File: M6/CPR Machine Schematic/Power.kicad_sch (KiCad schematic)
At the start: 51 parts, among them J1 Contactor 22.2V IN, J2 5V Spare Headers, J3 Power Switch, J4 3V3 Spare Headers, J5 12 Spare headers, J6 Battery Spare headers, J7 GND Spare Headers, Q1 2N3904, Q2 AO3407A, Q4 DMMT5401 PNP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

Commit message: PCB V2 Part 2
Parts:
- C1, C5, C7: footprint Capacitor_SMD:C_1206_3216Metric -> Capacitor_SMD:C_1206_3216Metric_Pad1.33x1.80mm_HandSolder; now left out of the parts list
- C10: footprint Capacitor_SMD:C_1206_3216Metric -> Capacitor_SMD:C_1206_3216Metric_Pad1.33x1.80mm_HandSolder; digikey (none) -> 311-4461-1-ND
- C11: footprint Capacitor_SMD:C_1206_3216Metric -> Capacitor_SMD:C_1206_3216Metric_Pad1.33x1.80mm_HandSolder; digikey (none) -> 732-8099-1-ND
- C12: footprint Capacitor_SMD:C_1206_3216Metric -> Capacitor_SMD:C_1206_3216Metric_Pad1.33x1.80mm_HandSolder; digikey (none) -> 732-8122-1-ND
- C2: footprint Capacitor_SMD:C_1206_3216Metric -> Capacitor_THT:CP_Radial_D10.0mm_P5.00mm; digikey (none) -> 565-EGXF161ELL510MJ20S-ND
- C3: footprint Capacitor_SMD:C_1206_3216Metric -> Capacitor_SMD:C_1206_3216Metric_Pad1.33x1.80mm_HandSolder; digikey (none) -> 399-C1206C220K5HACTUCT-ND
- C4, C6, C8, C9: footprint Capacitor_SMD:C_1206_3216Metric -> Capacitor_SMD:C_1206_3216Metric_Pad1.33x1.80mm_HandSolder; digikey (none) -> 1276-1072-1-ND
- D2: value B220 -> B220a; footprint Diode_SMD:D_SMB -> Diode_SMD:D_SMA_Handsoldering; digikey (none) -> B220A-FDICT-ND
- D3: footprint Diode_SMD:D_SMA -> Diode_SMD:D_SMB_Handsoldering; digikey (none) -> 1801-SS24CT-ND
- F1: footprint Fuse:Fuse_1206_3216Metric -> Fuse:Fuse_1206_3216Metric_Pad1.42x1.75mm_HandSolder; digikey (none) -> 5923-C1F5CT-ND
- J1, J3: digikey (none) -> 277-1667-ND
- J2, J4, J5, J6, J7, TP1, TP2, TP3, TP4: now left out of the parts list
- L1: digikey (none) -> 513-1432-1-ND
- L2: value 5 uH -> 6.8 uH; digikey (none) -> 118-SRU8043-6R8YCT-ND
- LED1, LED2, LED3, LED4: digikey (none) -> 160-1179-1-ND
- Q1: footprint Package_TO_SOT_THT:TO-92_Inline -> Package_TO_SOT_THT:TO-92_Inline_Wide; digikey (none) -> 2N3904FS-ND
- Q2: digikey (none) -> 785-1006-1-ND
- Q4: digikey (none) -> DMMT5401-FDICT-ND
- R1, R4: value 50 kOhm -> 49.9 kOhm; footprint Resistor_SMD:R_1206_3216Metric -> Resistor_SMD:R_1206_3216Metric_Pad1.30x1.75mm_HandSolder; digikey (none) -> 311-49.9KFRCT-ND
- R10: value 660 Ohm -> 665 Ohm; footprint Resistor_SMD:R_1206_3216Metric -> Resistor_SMD:R_1206_3216Metric_Pad1.30x1.75mm_HandSolder; digikey (none) -> 311-665FRCT-ND
- R11, R12, R13: footprint Resistor_SMD:R_1206_3216Metric -> Resistor_SMD:R_1206_3216Metric_Pad1.30x1.75mm_HandSolder; now left out of the parts list
- R14, R8: footprint Resistor_SMD:R_1206_3216Metric -> Resistor_SMD:R_1206_3216Metric_Pad1.30x1.75mm_HandSolder; digikey (none) -> A129830CT-ND
- R2: footprint Resistor_SMD:R_1206_3216Metric -> Resistor_SMD:R_1206_3216Metric_Pad1.30x1.75mm_HandSolder; digikey (none) -> 118-CR1206-FX-3571ELFCT-ND
- R3: footprint Resistor_SMD:R_1206_3216Metric -> Resistor_SMD:R_1206_3216Metric_Pad1.30x1.75mm_HandSolder; digikey (none) -> RMCF1206FT20K0CT-ND
- R7: footprint Resistor_SMD:R_1206_3216Metric -> Resistor_SMD:R_1206_3216Metric_Pad1.30x1.75mm_HandSolder; digikey (none) -> RMCF1206FT2K00CT-ND
- R9: value 1.4 kOhm -> 1.5 kOhm; footprint Resistor_SMD:R_1206_3216Metric -> Resistor_SMD:R_1206_3216Metric_Pad1.30x1.75mm_HandSolder; digikey (none) -> RMCF1206JG1K50CT-ND
- U1: digikey (none) -> 505-LT1765EFE-5#PBF-ND
- U2: digikey (none) -> 505-MAX42402AFLB+-ND
- U4: digikey (none) -> 1951-2739-ND
- U6: digikey (none) -> 1951-2742-ND

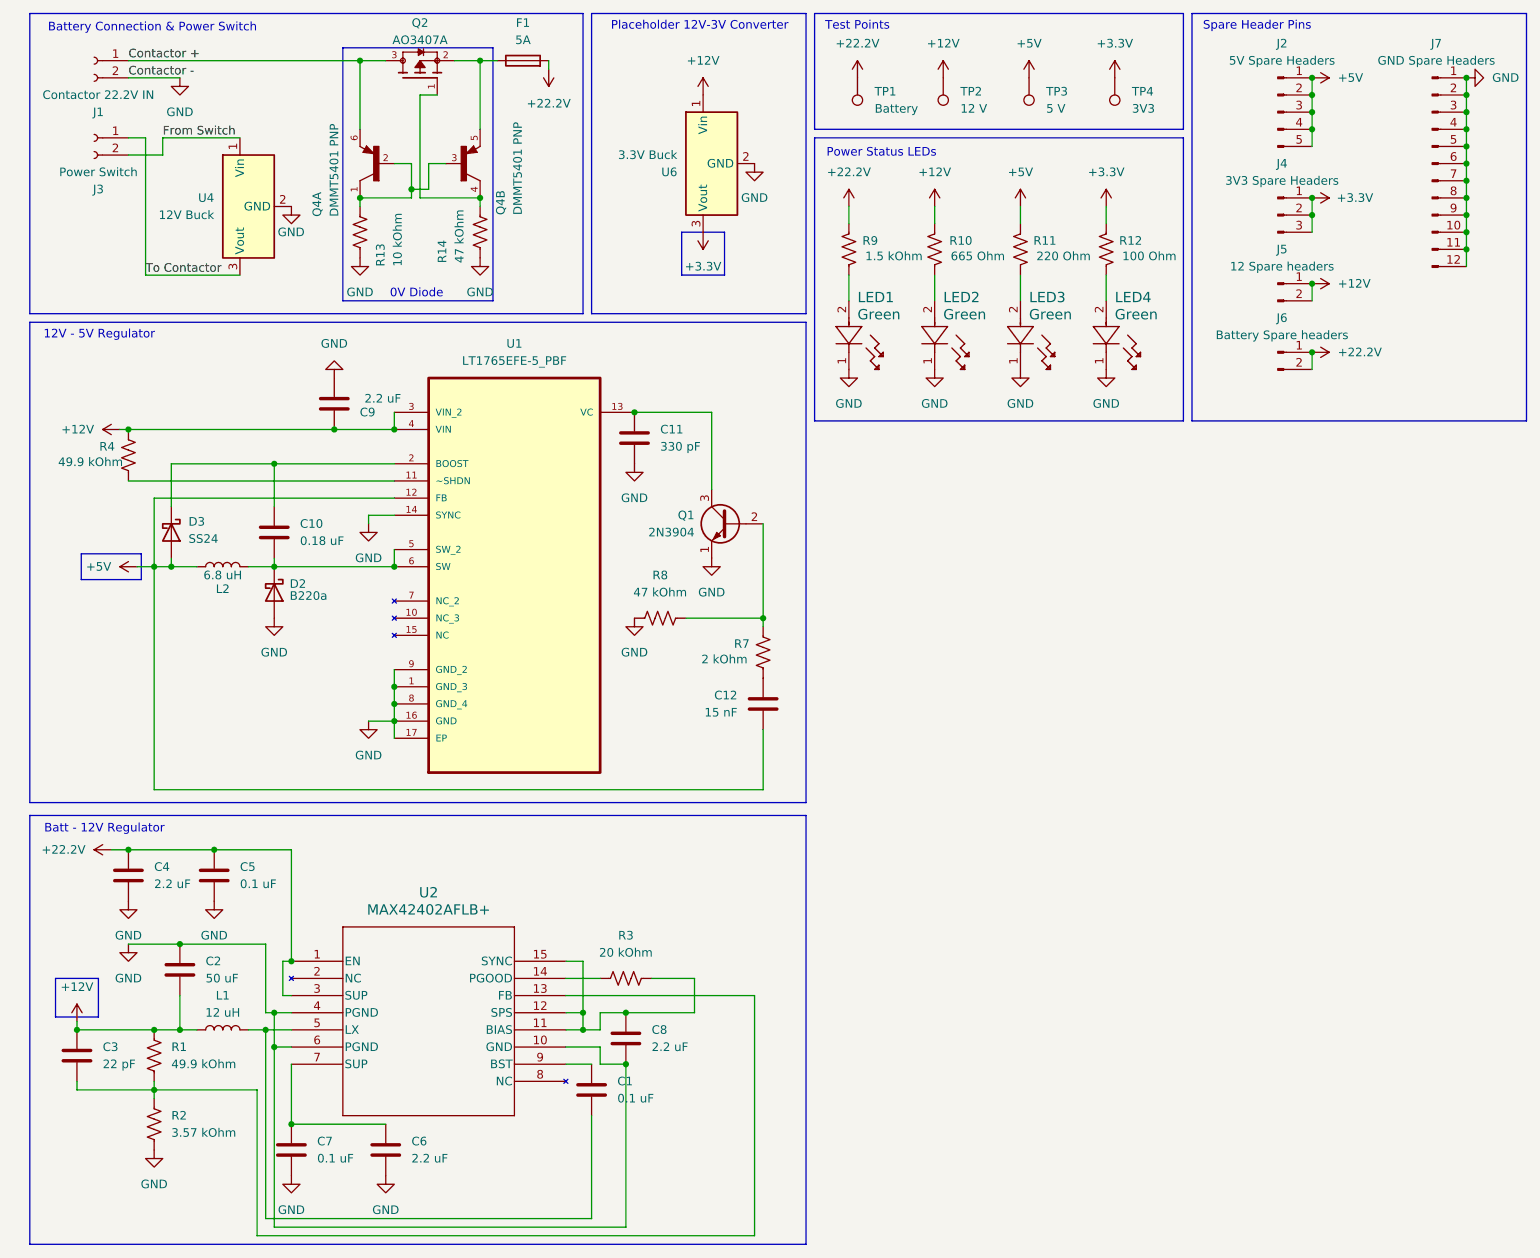
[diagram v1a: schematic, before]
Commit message: Down with the second buck converter
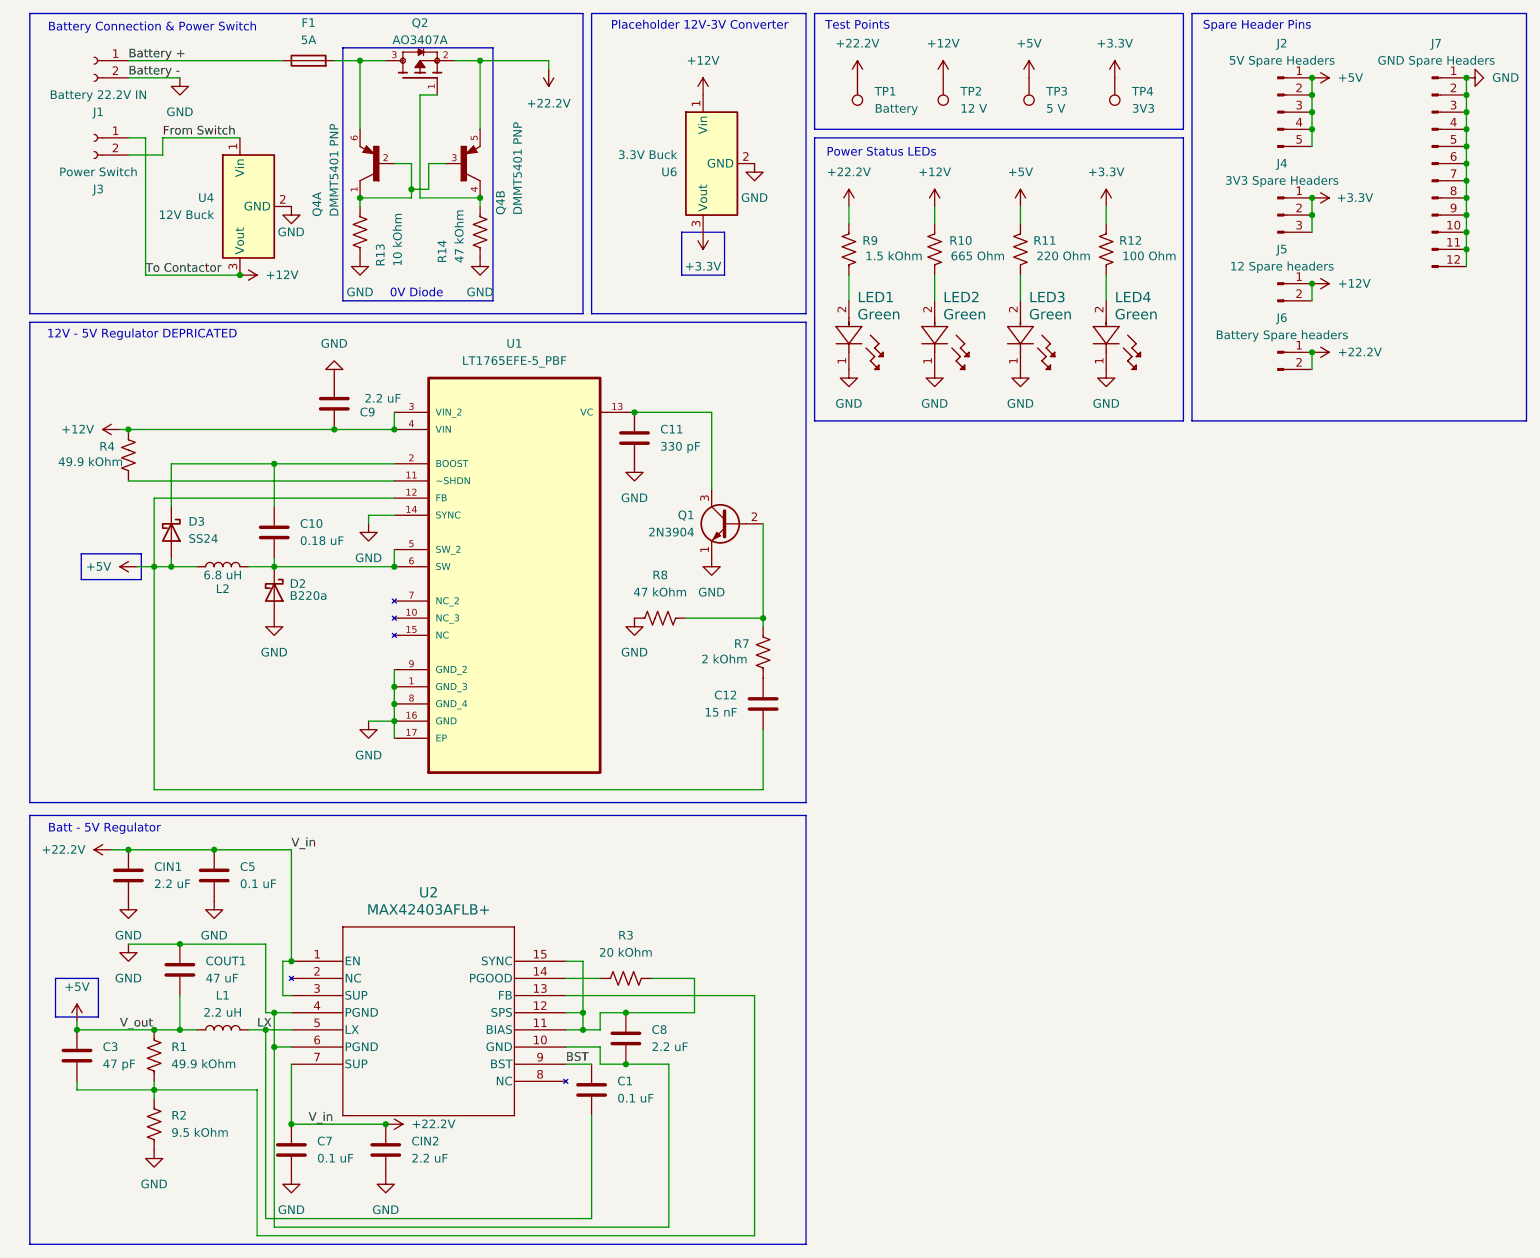
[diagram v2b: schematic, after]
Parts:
- C1, C5, C7: digikey (none) -> 490-GRM3195C1H104JA05DCT-ND
- C10, C11, C12, C9, D2, D3, L2, Q1, R4, R7, R8, U1: now left out of the parts list
- C3: value 22 pF -> 47 pF; digikey 399-C1206C220K5HACTUCT-ND -> 1292-1206N470J102CT-ND
- C8: digikey 1276-1072-1-ND -> 490-17674-1-ND
- CIN1: renamed from C4; digikey 1276-1072-1-ND -> 490-17674-1-ND
- CIN2: renamed from C6; digikey 1276-1072-1-ND -> 490-17674-1-ND
- COUT1: renamed from C2; value 50 uF -> 47 uF; footprint Capacitor_THT:CP_Radial_D10.0mm_P5.00mm -> Capacitor_THT:CP_Radial_D8.0mm_P3.50mm; digikey 565-EGXF161ELL510MJ20S-ND -> 732-6324-1-ND
- J1: value Contactor 22.2V IN -> Battery 22.2V IN
- L1: value 12 uH -> 2.2 uH; footprint DR124_120_R:IND_CB_DR124 -> Imports:IND_1217AS-H-2R2N=P3; digikey 513-1432-1-ND -> 490-10787-1-ND
- Q2: footprint Package_TO_SOT_SMD:SOT-23-3 -> Package_TO_SOT_SMD:SOT-23_Handsoldering
- R2: value 3.57 kOhm -> 9.5 kOhm; digikey 118-CR1206-FX-3571ELFCT-ND -> 311-9.53KFRCT-ND
- U2: value MAX42402AFLB+ -> MAX42403AFLB+; digikey 505-MAX42402AFLB+-ND -> 505-MAX42403AFLB+-ND
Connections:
- net To Contactor is gone; now on net +12V: J3.1 (Pin_1), U4.3 (Vout)
- net +12V: no longer C3.2, COUT1.1, L1.1, R1.1
- net +22.2V: now also C7.2, CIN2.2, Q2.2, Q4.5, U2.7 (SUP); no longer F1.2
- net +5V: now also C3.2, COUT1.1, L1.1, R1.1
- net LX: now reaches C1.1, L1.2, U2.5 (LX)
- net BST: now reaches C1.2, U2.9 (BST)
- net Contactor +: no longer names the net of Q2.3, Q4.6
- net Contactor +: now also F1.2; no longer J1.1 (Pin_1)
- new net Battery +: F1.1, J1.1 (Pin_1)
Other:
- note added: "12V - 5V Regulator DEPRICATED"
- note added: "Batt - 5V Regulator"
- note removed: "12V - 5V Regulator"
- note removed: "Batt - 12V Regulator"
- moved on the sheet: F1
